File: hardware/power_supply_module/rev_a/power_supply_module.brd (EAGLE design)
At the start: 68.1 x 66 mm, 73 parts, among them J1 MODULE_POWER, U1 TLV62130, U10 LTC2941, U11 LTC2941, U12 LTC2941, U13 LTC2941, U14 LTC2941, U15 LTC2941, U2 TLV62130, U3 TLV62130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

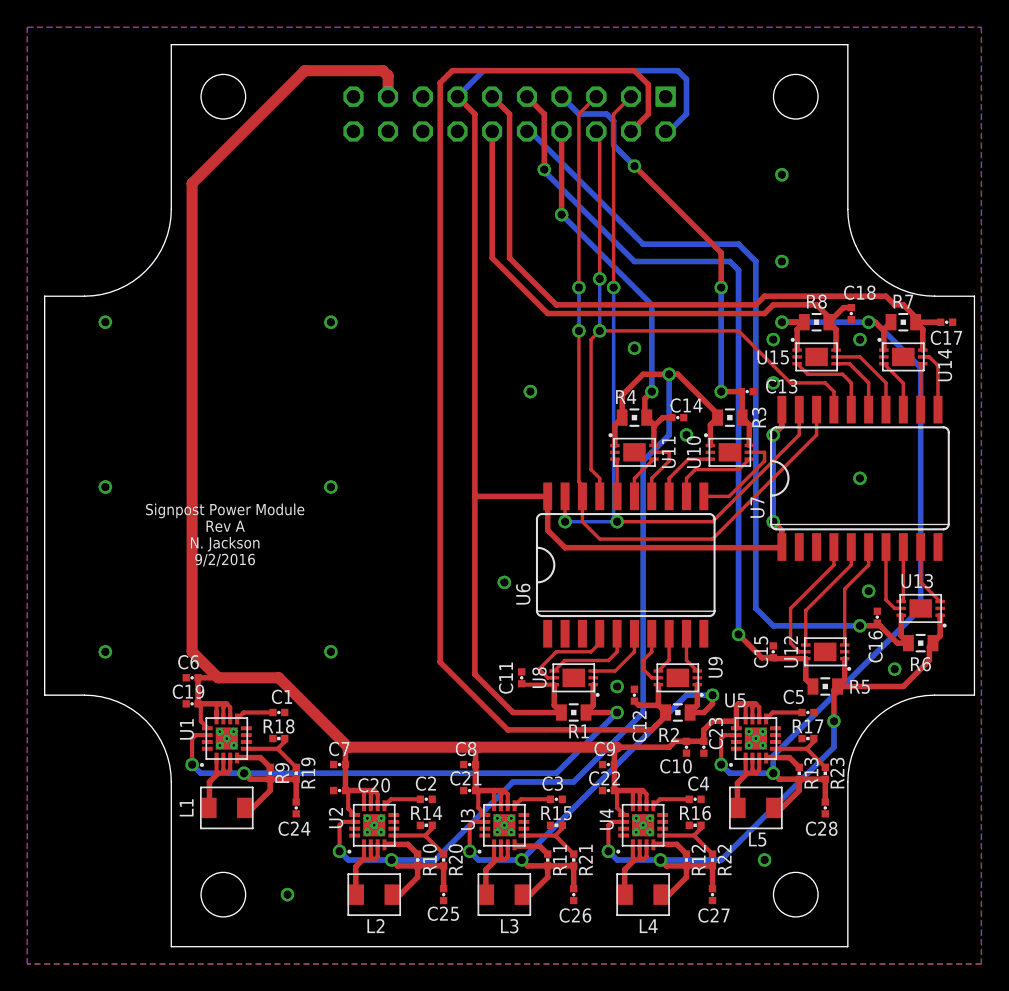
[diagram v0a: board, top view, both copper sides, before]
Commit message: Increased trace widths for high current signals
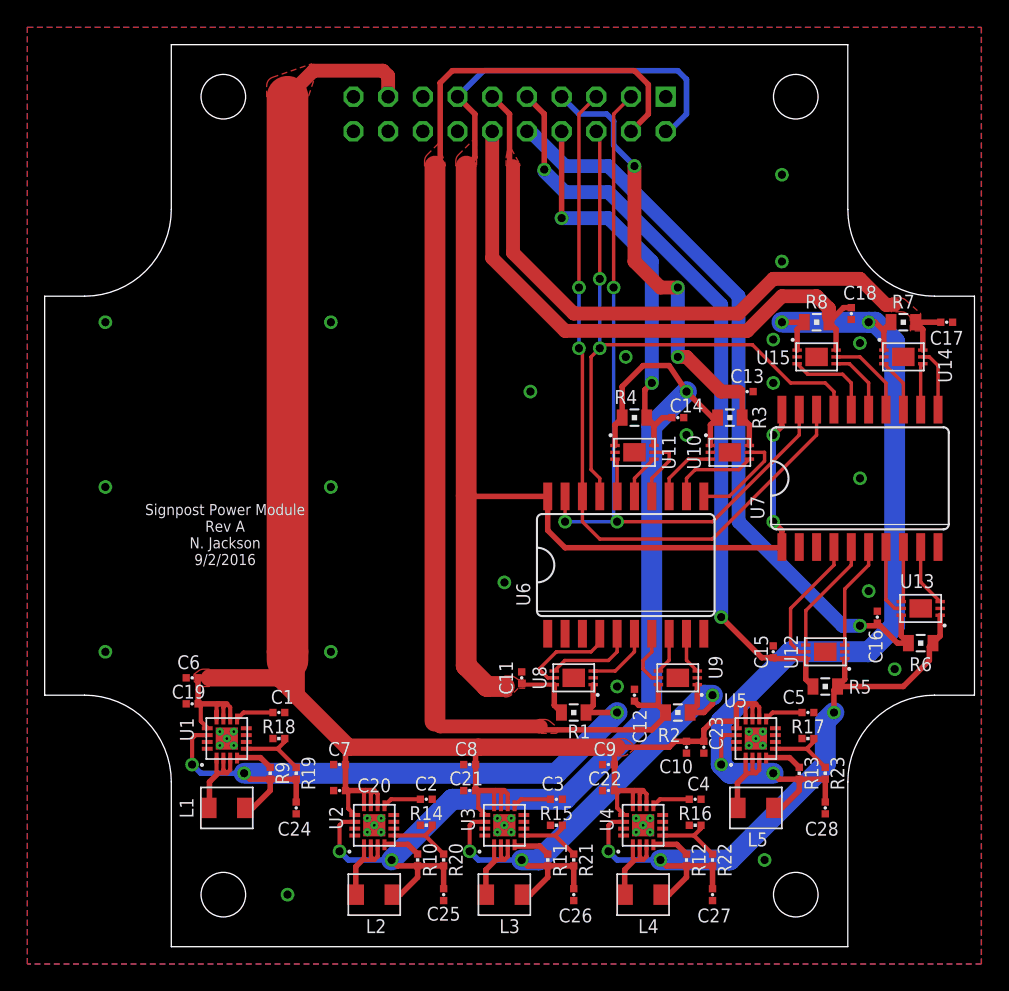
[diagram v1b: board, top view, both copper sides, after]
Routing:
- net VCC_MOD5: track 60.9 -> 55.7 mm
- net VCC_BACKPLANE: track 113.5 -> 109.7 mm
- net VCC_LINUX: track 85.8 -> 89.0 mm
- net VBATT: track 151.1 -> 148.2 mm
- net 5V_4: track 69.3 -> 72.0 mm
- net VCC_MOD2: track 57.8 -> 55.6 mm
- net VCC_MOD1: track 27.8 -> 29.8 mm
- net VCC_MOD7: track 40.9 -> 42.9 mm
- net VCC_MOD0: track 33.3 -> 34.4 mm
- net 5V_2: track 79.7 -> 80.6 mm
- net VCC_MOD6: track 48.9 -> 48.2 mm
- added copper zone on layer 1, net VBATT
- added copper zone on layer 1, net VCC_BACKPLANE
- added copper zone on layer 1, net VCC_LINUX
- added copper zone on layer 1, net VCC_MOD6

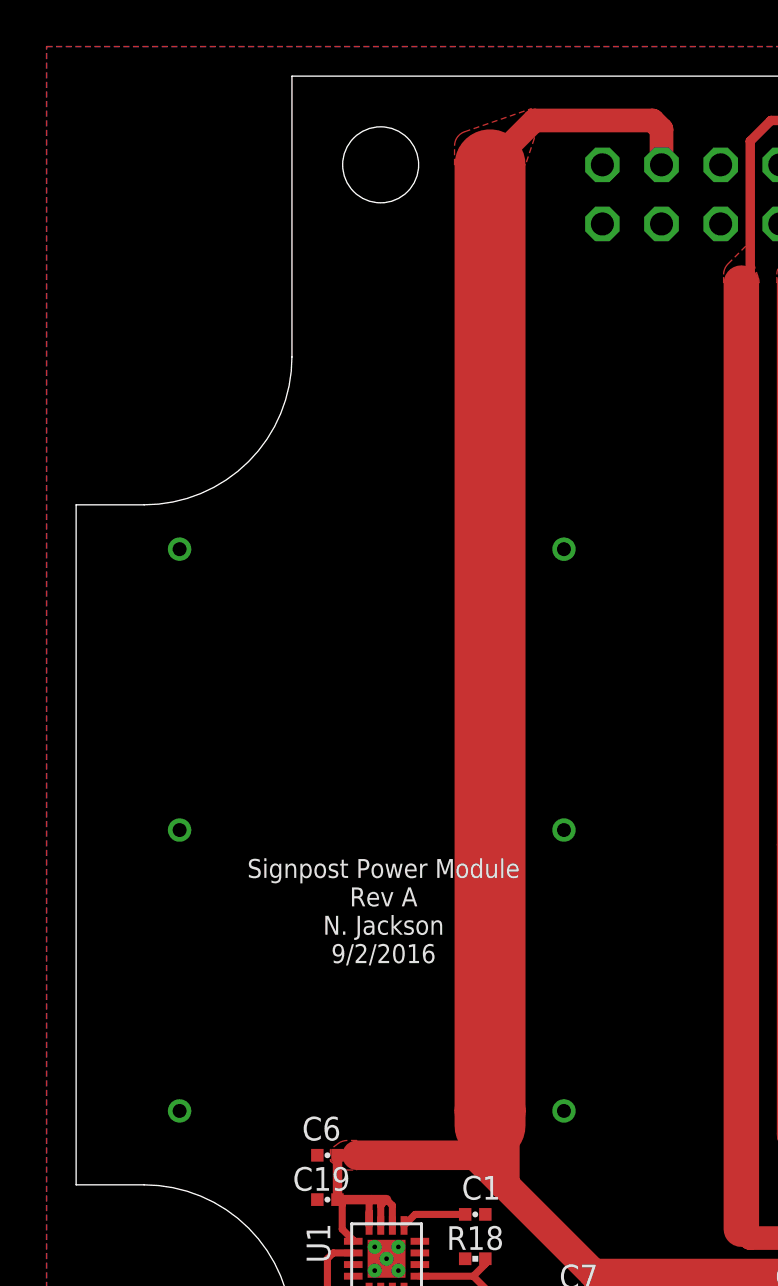
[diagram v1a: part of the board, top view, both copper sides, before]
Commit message: Added breakouts for solar panel, battery
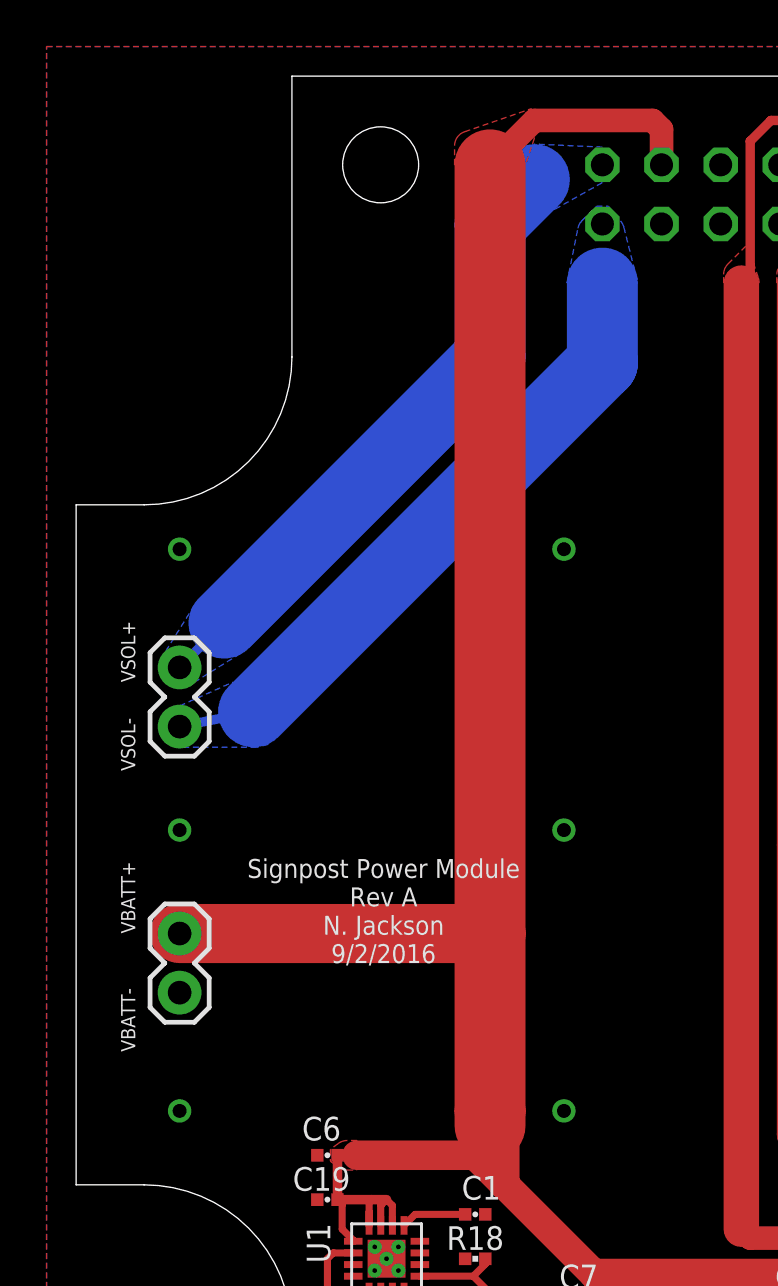
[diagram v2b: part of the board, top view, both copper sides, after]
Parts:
- added JP1, JP2: (no value), SparkFun-Connectors:1X02
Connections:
- net GND: now also JP2.1
- net VBATT: now also JP2.2
- net VSOL+: now also JP1.2
- net VSOL-: now also JP1.1
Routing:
- net VSOL-: track 0.00 -> 27.9 mm
- net VSOL+: track 0.00 -> 27.3 mm
- net VBATT: track 148.2 -> 161.5 mm
- added copper zone on layer 16, net VSOL+
- added copper zone on layer 16, net VSOL-
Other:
- board text added: "VBATT+"
- board text added: "VBATT-"
- board text added: "VSOL+"
- board text added: "VSOL-"
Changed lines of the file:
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@@
 N. Jackson
 9/2/2016</text>
+<text x="2.54" y="40.005" size="0.6096" layer="112" font="vector" rot="R90">VSOL+</text>
+<text x="2.54" y="36.195" size="0.6096" layer="112" font="vector" rot="R90">VSOL-</text>
+<text x="2.54" y="24.13" size="0.6096" layer="112" font="vector" rot="R90">VBATT-</text>
+<text x="2.54" y="29.21" size="0.6096" layer="112" font="vector" rot="R90">VBATT+</text>
 </plain>
 <attributes>
@@
 </element>
 <element name="U$1" library="logos" package="UCB_CAL_350MIL" value="" x="7.62" y="33.02"/>
+<element name="JP1" library="SparkFun-Connectors" package="1X02" value="" x="4.445" y="38.1" smashed="yes" rot="R90">
+<attribute name="VALUE" x="7.62" y="36.83" size="1.27" layer="27" rot="R90"/>
+</element>
+<element name="JP2" library="SparkFun-Connectors" package="1X02" value="" x="4.445" y="26.67" smashed="yes" rot="R90">
+<attribute name="VALUE" x="7.62" y="25.4" size="1.27" layer="27" rot="R90"/>
+</element>
 </elements>
 <signals>
-<signal name="VSOL+">
-<contactref element="J1" pad="19"/>
-</signal>
-<signal name="VSOL-">
-<contactref element="J1" pad="20"/>
-</signal>
 <signal name="GND">
 <contactref element="J1" pad="18"/>
@@
 <vertex x="-1.27" y="-1.27"/>
 </polygon>
-<polygon width="0.4064" layer="16">
+<polygon width="0.4064" layer="16" rank="2">
 <vertex x="-1.27" y="67.31"/>
 <vertex x="68.58" y="67.31"/>
@@
 <via x="52.705" y="6.35" extent="1-16" drill="0.6"/>
 <via x="62.23" y="20.32" extent="1-16" drill="0.6"/>
+<contactref element="JP2" pad="1"/>
 </signal>
 <signal name="VCC_BACKPLANE">
@@
 <wire x1="46.15306875" y1="15.03806875" x2="45.72" y2="14.605" width="0.4064" layer="1"/>
 <wire x1="45.72" y1="14.605" x2="41.91" y2="14.605" width="0.4064" layer="1"/>
-<wire x1="17.78" y1="62.23" x2="17.78" y2="21.59" width="3.048" layer="1"/>
+<wire x1="17.78" y1="62.23" x2="17.78" y2="29.21" width="3.048" layer="1"/>
+<wire x1="17.78" y1="29.21" x2="17.78" y2="21.59" width="3.048" layer="1"/>
 <wire x1="17.78" y1="21.59" x2="17.78" y2="20.955" width="3.048" layer="1"/>
 <wire x1="11.22806875" y1="19.685" x2="12.065" y2="19.685" width="0.4064" layer="1"/>
@@
 <vertex x="41.91" y="13.97"/>
 </polygon>
+<contactref element="JP2" pad="2"/>
+<wire x1="4.445" y1="29.21" x2="17.78" y2="29.21" width="2.54" layer="1"/>
 </signal>
 <signal name="VCC_LINUX">
@@
 <via x="53.975" y="56.515" extent="1-16" drill="0.6"/>
 </signal>
+<signal name="VSOL+">
+<contactref element="J1" pad="19"/>
+<contactref element="JP1" pad="2"/>
+<wire x1="19.685" y1="61.595" x2="17.78" y2="59.69" width="3.048" layer="16"/>
+<wire x1="17.78" y1="59.69" x2="17.78" y2="53.975" width="3.048" layer="16"/>
+<wire x1="17.78" y1="53.975" x2="6.35" y2="42.545" width="3.048" layer="16"/>
+<polygon width="0" layer="16" thermals="no">
+<vertex x="7.112" y="41.275"/>
+<vertex x="5.08" y="43.307"/>
+<vertex x="3.81" y="41.275"/>
+<vertex x="3.81" y="40.005"/>
+<vertex x="5.08" y="40.005"/>
+</polygon>
+<wire x1="4.445" y1="40.64" x2="6.35" y2="42.545" width="0.4064" layer="16"/>
+<polygon width="0" layer="16" thermals="no">
+<vertex x="22.606" y="62.992"/>
+<vertex x="19.685" y="63.119"/>
+<vertex x="19.685" y="60.325"/>
+<vertex x="20.574" y="60.325"/>
+<vertex x="22.606" y="61.468"/>
+</polygon>
+</signal>
+<signal name="VSOL-">
+<contactref element="J1" pad="20"/>
+<contactref element="JP1" pad="1"/>
+<wire x1="22.606" y1="53.721" x2="7.62" y2="38.735" width="3.048" layer="16"/>
+<wire x1="22.606" y1="53.721" x2="22.606" y2="57.15" width="3.048" layer="16"/>
+<polygon width="0" layer="16" thermals="no">
+<vertex x="4.445" y="38.989"/>
+<vertex x="6.731" y="40.005"/>
+<vertex x="8.255" y="37.338"/>
+<vertex x="7.747" y="37.211"/>
+<vertex x="4.445" y="37.211"/>
+<vertex x="3.81" y="37.465"/>
+<vertex x="3.81" y="38.735"/>
+</polygon>
+<wire x1="4.445" y1="38.1" x2="7.62" y2="38.735" width="0.4064" layer="16"/>
+<polygon width="0" layer="16" thermals="no">
+<vertex x="21.082" y="57.15"/>
+<vertex x="21.55229375" y="59.50146875" curve="-33.690212"/>
+<vertex x="21.72595" y="59.82595"/>
+<vertex x="22.352" y="60.452"/>
+<vertex x="22.86" y="60.452"/>
+<vertex x="23.402009375" y="59.8015875" curve="-25.768611"/>
+<vertex x="23.530228125" y="59.5490875"/>
+<vertex x="24.13" y="57.15"/>
+</polygon>
+</signal>
 </signals>

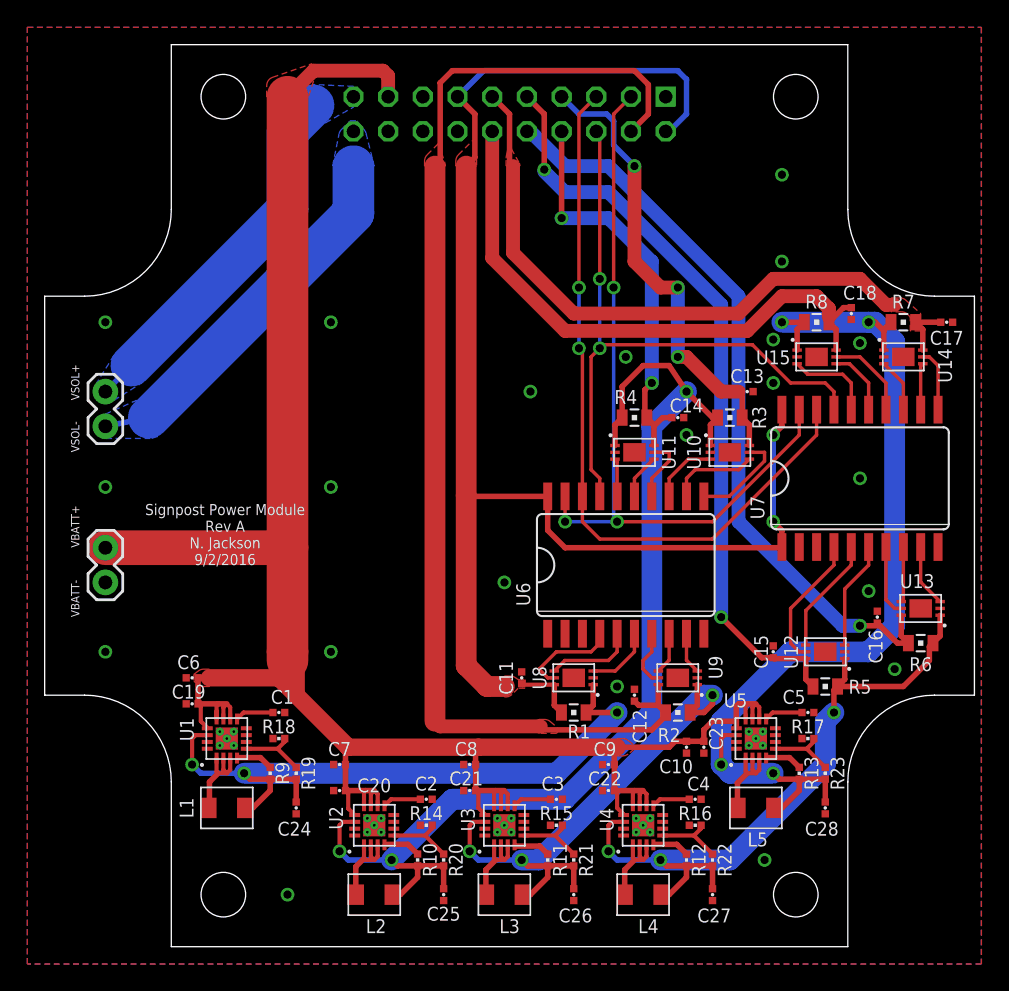
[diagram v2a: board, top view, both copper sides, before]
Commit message: Added testpoints for rails, signals to modules/linux/backplane/controller, smbus
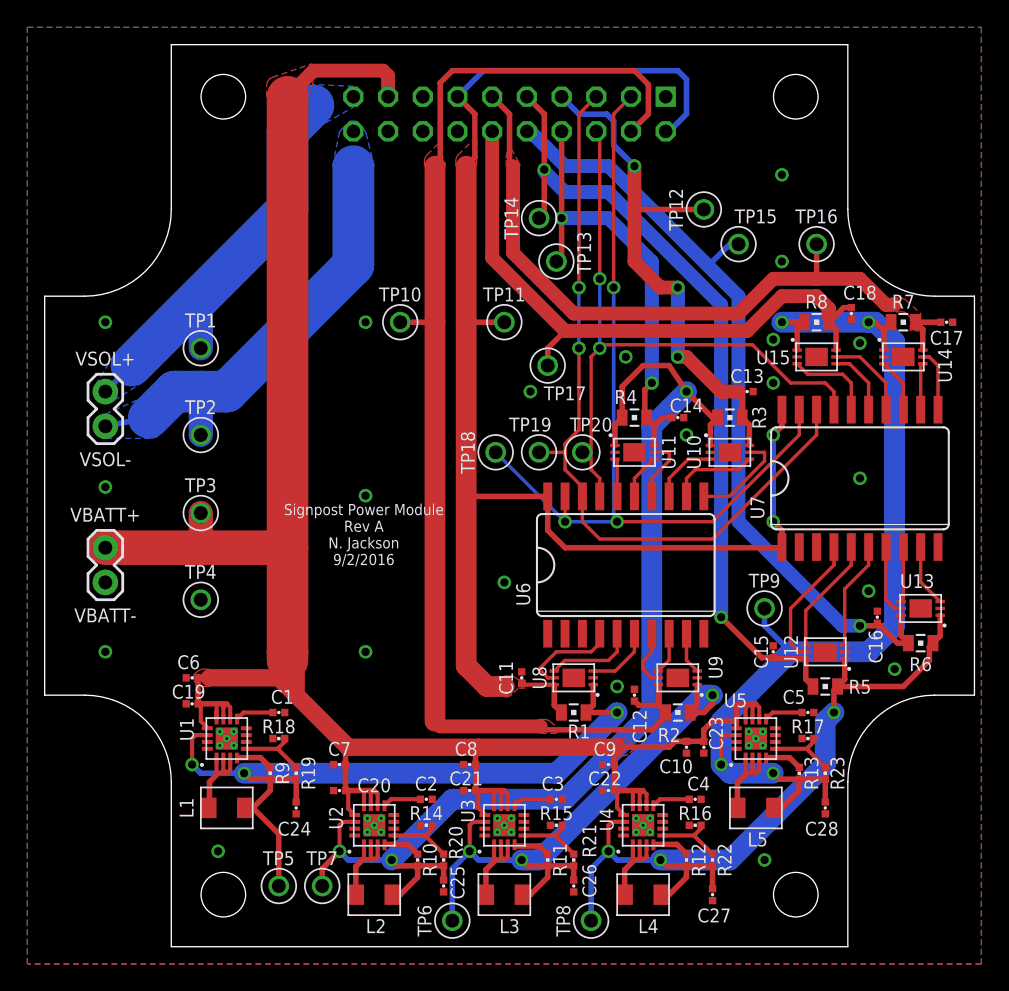
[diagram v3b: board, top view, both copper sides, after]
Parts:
- added TP1, TP10, TP11, TP12, TP13, TP14, TP15, TP16, TP17, TP18, TP19, TP2, TP20, TP3, TP4, TP5, TP6, TP7, TP8, TP9: TEST_POINT_0.040IN, headers:TESTPOINT_0.040IN
- moved U$1 10.2 mm to (17.8, 33.7)
- moved C25 0.64 mm to (29.2, 4.45)
- moved C26 0.64 mm to (38.7, 4.45)
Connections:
- net !INT: now also TP20.TESTPOINT
- net 3V3: now also TP5.TESTPOINT
- net 5V_1: now also TP6.TESTPOINT
- net 5V_2: now also TP7.TESTPOINT
- net 5V_3: now also TP8.TESTPOINT
- net 5V_4: now also TP9.TESTPOINT
- net GND: now also TP4.TESTPOINT
- net SCL: now also TP19.TESTPOINT
- net SDA: now also TP18.TESTPOINT
- net VBATT: now also TP3.TESTPOINT
- net VCC_BACKPLANE: now also TP11.TESTPOINT
- net VCC_LINUX: now also TP10.TESTPOINT
- net VCC_MOD0: now also TP12.TESTPOINT
- net VCC_MOD1: now also TP13.TESTPOINT
- net VCC_MOD2: now also TP14.TESTPOINT
- net VCC_MOD5: now also TP15.TESTPOINT
- net VCC_MOD6: now also TP16.TESTPOINT
- net VCC_MOD7: now also TP17.TESTPOINT
- net VSOL+: now also TP1.TESTPOINT
- net VSOL-: now also TP2.TESTPOINT
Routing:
- net SDA: track 55.2 -> 62.4 mm
- net 3V3: track 49.7 -> 56.2 mm
- net 5V_3: track 50.5 -> 56.1 mm
- net VSOL-: track 27.9 -> 33.3 mm
- net VCC_MOD0: track 34.4 -> 39.5 mm
- net 5V_1: track 39.8 -> 44.8 mm
- net 5V_4: track 72.0 -> 76.0 mm
- net VSOL+: track 27.3 -> 31.1 mm
- net VCC_MOD2: track 55.6 -> 59.3 mm
- net VCC_MOD1: track 29.8 -> 33.1 mm
- net VCC_MOD7: track 42.9 -> 46.0 mm
- net VCC_MOD5: track 55.7 -> 58.5 mm
- net VCC_BACKPLANE: track 109.7 -> 112.5 mm
- net SCL: track 54.4 -> 57.2 mm
- net VCC_MOD6: track 48.2 -> 50.7 mm
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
